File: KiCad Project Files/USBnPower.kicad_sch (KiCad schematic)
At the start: 11 parts, among them J1 SM04B, U3 XC6206PxxxMR, U4 PRTR5V0U2X

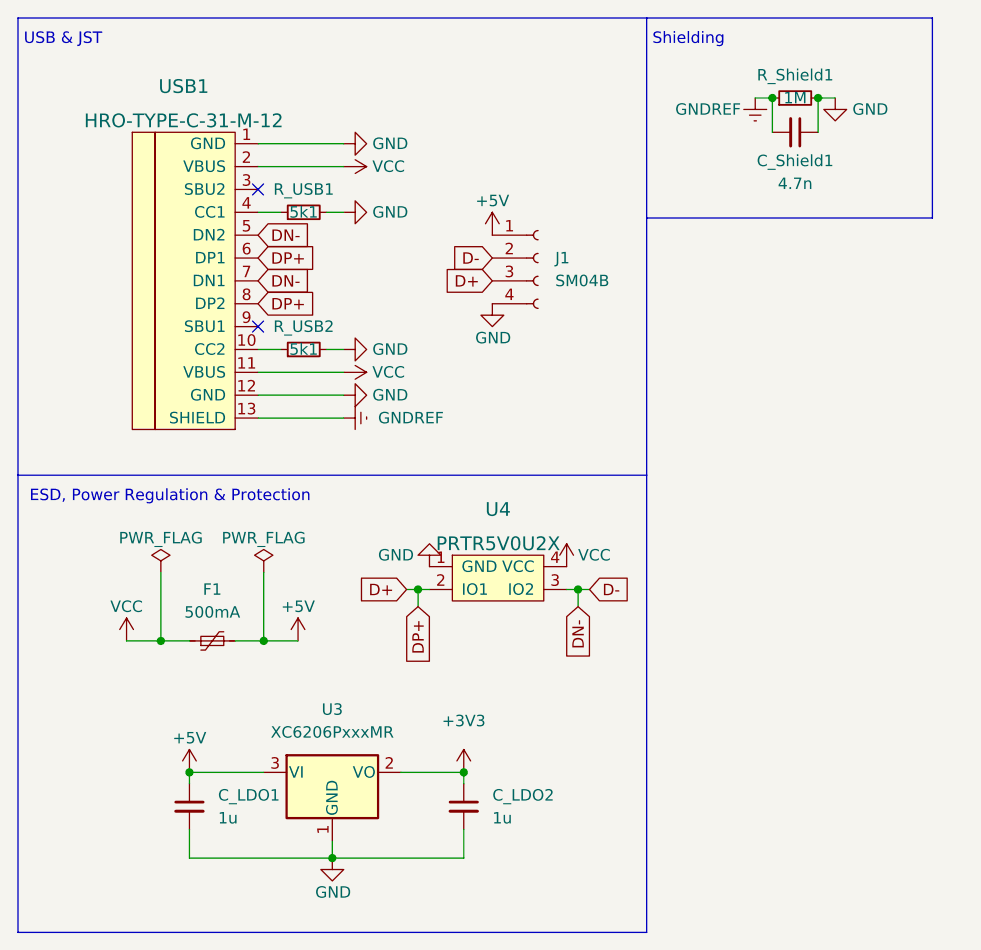
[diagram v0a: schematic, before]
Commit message: begin work on stm32 branch
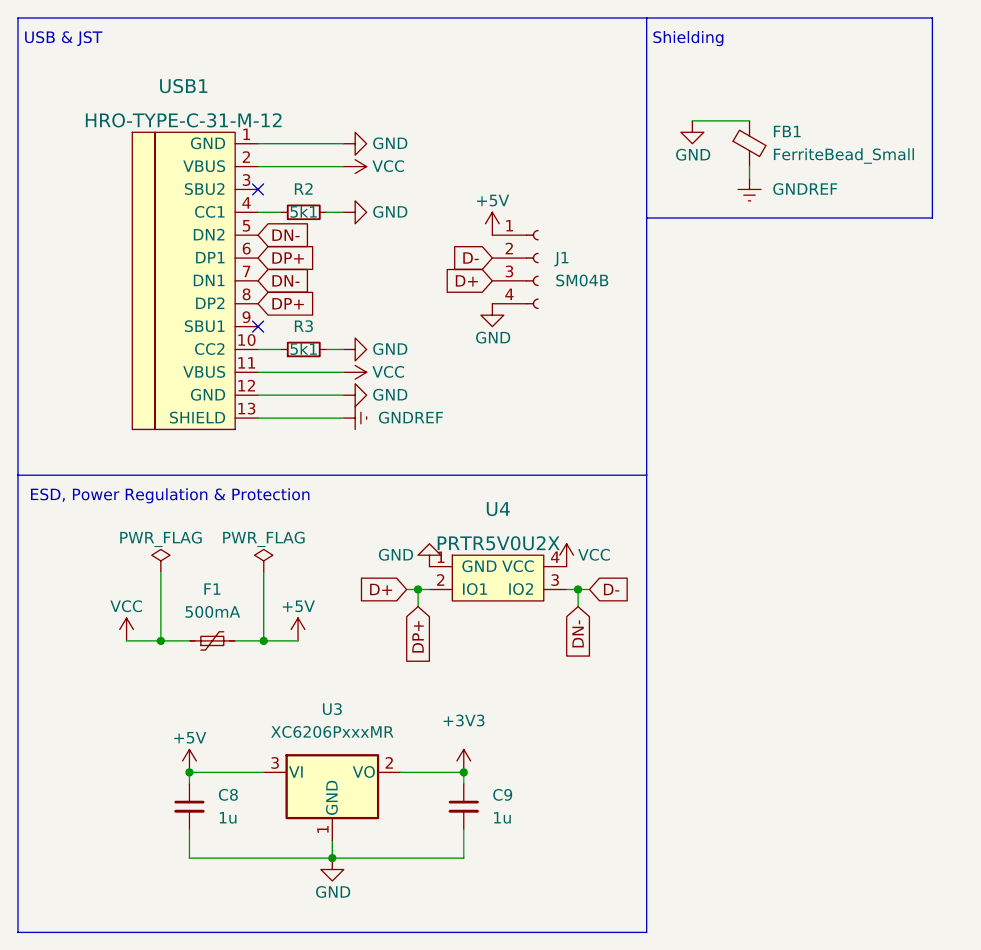
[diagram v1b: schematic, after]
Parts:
- removed C_Shield1: 4.7n, Capacitor_SMD:C_0402_1005Metric, symbol Device:C_Small
- removed R_Shield1: 1M, Resistor_SMD:R_0402_1005Metric, symbol Device:R_Small
- added FB1: FerriteBead_Small, Inductor_SMD:L_0805_2012Metric, symbol Device:FerriteBead_Small
- renumbered C_LDO1 to C8, C_LDO2 to C9, R_USB1 to R2, R_USB2 to R3
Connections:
- net GND: now also FB1.1
- net GNDREF: now also FB1.2
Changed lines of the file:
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@@
 (kicad_sch (version 20211123) (generator eeschema)
   (paper "A5")
-  (junction (at 96.52 21.59) (diameter 0) (color 0 0 0 0)
-  )
   (junction (at 40.005 81.915) (diameter 0) (color 0 0 0 0)
   )
@@
   )
   (junction (at 74.93 76.2) (diameter 0) (color 0 0 0 0)
-  )
-  (junction (at 101.6 21.59) (diameter 0) (color 0 0 0 0)
   )
   (junction (at 47.625 106.045) (diameter 0) (color 0 0 0 0)
@@
     (stroke (width 0) (type default) (color 0 0 0 0))
   )
-  (wire (pts (xy 96.52 21.59) (xy 96.52 25.4))
-    (stroke (width 0) (type default) (color 0 0 0 0))
-  )
   (wire (pts (xy 47.625 104.14) (xy 47.625 106.045))
     (stroke (width 0) (type default) (color 0 0 0 0))
@@
     (stroke (width 0) (type default) (color 0 0 0 0))
   )
-  (wire (pts (xy 101.6 21.59) (xy 101.6 25.4))
-    (stroke (width 0) (type default) (color 0 0 0 0))
-  )
   (polyline (pts (xy 12.7 12.7) (xy 12.7 63.5))
     (stroke (width 0) (type default) (color 0 0 0 0))
@@
     (stroke (width 0) (type default) (color 0 0 0 0))
   )
-  (wire (pts (xy 101.6 21.59) (xy 103.505 21.59))
-    (stroke (width 0) (type default) (color 0 0 0 0))
-  )
   (polyline (pts (xy 82.55 114.3) (xy 12.7 114.3))
     (stroke (width 0) (type default) (color 0 0 0 0))
@@
     (stroke (width 0) (type default) (color 0 0 0 0))
   )
-  (wire (pts (xy 94.615 21.59) (xy 96.52 21.59))
+  (wire (pts (xy 93.98 29.21) (xy 93.98 30.48))
     (stroke (width 0) (type default) (color 0 0 0 0))
   )
@@
   )
   (wire (pts (xy 74.93 76.2) (xy 76.2 76.2))
+    (stroke (width 0) (type default) (color 0 0 0 0))
+  )
+  (wire (pts (xy 87.63 24.13) (xy 93.98 24.13))
     (stroke (width 0) (type default) (color 0 0 0 0))
   )
@@
   (symbol (lib_id "Device:R_Small") (at 44.45 49.53 90) (unit 1)
     (in_bom yes) (on_board yes)
-    (property "Reference" "R_USB2" (id 0) (at 44.45 46.99 90))
+    (property "Reference" "R3" (id 0) (at 44.45 46.99 90))
     (property "Value" "5k1" (id 1) (at 44.45 49.53 90))
     (property "Footprint" "Resistor_SMD:R_0402_1005Metric" (id 2) (at 44.45 49.53 0)
@@
     (pin "2")
   )
-  (symbol (lib_id "power:GNDREF") (at 94.615 21.59 0) (unit 1)
-    (in_bom yes) (on_board yes)
-    (property "Reference" "#PWR0132" (id 0) (at 94.615 27.94 0)
-      (effects (font (size 1.27 1.27)) hide)
-    )
-    (property "Value" "GNDREF" (id 1) (at 85.725 22.86 0)
-      (effects (font (size 1.27 1.27)) (justify left))
-    )
-    (property "Footprint" "" (id 2) (at 94.615 21.59 0)
-      (effects (font (size 1.27 1.27)) hide)
-    )
-    (property "Datasheet" "" (id 3) (at 94.615 21.59 0)
-      (effects (font (size 1.27 1.27)) hide)
-    )
-    (pin "1")
-  )
   (symbol (lib_id "power:GND") (at 58.42 73.66 180) (unit 1)
     (in_bom yes) (on_board yes)
@@
   (symbol (lib_id "Device:R_Small") (at 44.45 34.29 90) (unit 1)
     (in_bom yes) (on_board yes)
-    (property "Reference" "R_USB1" (id 0) (at 44.45 31.75 90))
+    (property "Reference" "R2" (id 0) (at 44.45 31.75 90))
     (property "Value" "5k1" (id 1) (at 44.45 34.29 90))
     (property "Footprint" "Resistor_SMD:R_0402_1005Metric" (id 2) (at 44.45 34.29 0)
@@
     )
     (property "Datasheet" "" (id 3) (at 48.895 57.15 0)
+      (effects (font (size 1.27 1.27)) hide)
+    )
+    (pin "1")
+  )
+  (symbol (lib_id "Device:FerriteBead_Small") (at 93.98 26.67 0) (unit 1)
+    (in_bom yes) (on_board yes) (fields_autoplaced)
+    (property "Reference" "FB1" (id 0) (at 96.52 25.3618 0)
+      (effects (font (size 1.27 1.27)) (justify left))
+    )
+    (property "Value" "FerriteBead_Small" (id 1) (at 96.52 27.9018 0)
+      (effects (font (size 1.27 1.27)) (justify left))
+    )
+    (property "Footprint" "Inductor_SMD:L_0805_2012Metric" (id 2) (at 92.202 26.67 90)
+      (effects (font (size 1.27 1.27)) hide)
+    )
+    (property "Datasheet" "~" (id 3) (at 93.98 26.67 0)
+      (effects (font (size 1.27 1.27)) hide)
+    )
+    (pin "1")
+    (pin "2")
+  )
+  (symbol (lib_id "power:GNDREF") (at 93.98 30.48 0) (unit 1)
+    (in_bom yes) (on_board yes) (fields_autoplaced)
+    (property "Reference" "#PWR0109" (id 0) (at 93.98 36.83 0)
+      (effects (font (size 1.27 1.27)) hide)
+    )
+    (property "Value" "GNDREF" (id 1) (at 96.52 31.7499 0)
+      (effects (font (size 1.27 1.27)) (justify left))
+    )
+    (property "Footprint" "" (id 2) (at 93.98 30.48 0)
+      (effects (font (size 1.27 1.27)) hide)
+    )
+    (property "Datasheet" "" (id 3) (at 93.98 30.48 0)
       (effects (font (size 1.27 1.27)) hide)
     )
@@
     (pin "1")
   )
-  (symbol (lib_id "Device:C_Small") (at 99.06 25.4 270) (unit 1)
-    (in_bom yes) (on_board yes)
-    (property "Reference" "C_Shield1" (id 0) (at 99.06 28.575 90))
-    (property "Value" "4.7n" (id 1) (at 99.06 31.115 90))
-    (property "Footprint" "Capacitor_SMD:C_0402_1005Metric" (id 2) (at 99.06 25.4 0)
-      (effects (font (size 1.27 1.27)) hide)
-    )
-    (property "Datasheet" "~" (id 3) (at 99.06 25.4 0)
-      (effects (font (size 1.27 1.27)) hide)
-    )
-    (pin "1")
-    (pin "2")
+  (symbol (lib_id "power:GND") (at 87.63 24.13 0) (unit 1)
+    (in_bom yes) (on_board yes)
+    (property "Reference" "#PWR0110" (id 0) (at 87.63 30.48 0)
+      (effects (font (size 1.27 1.27)) hide)
+    )
+    (property "Value" "GND" (id 1) (at 85.725 27.94 0)
+      (effects (font (size 1.27 1.27)) (justify left))
+    )
+    (property "Footprint" "" (id 2) (at 87.63 24.13 0)
+      (effects (font (size 1.27 1.27)) hide)
+    )
+    (property "Datasheet" "" (id 3) (at 87.63 24.13 0)
+      (effects (font (size 1.27 1.27)) hide)
+    )
+    (pin "1")
   )
   (symbol (lib_id "power:GND") (at 48.895 34.29 90) (unit 1)
@@
   (symbol (lib_id "Device:C_Small") (at 31.75 100.33 0) (unit 1)
     (in_bom yes) (on_board yes) (fields_autoplaced)
-    (property "Reference" "C_LDO1" (id 0) (at 34.925 99.0662 0)
+    (property "Reference" "C8" (id 0) (at 34.925 99.0662 0)
       (effects (font (size 1.27 1.27)) (justify left))
     )
@@
     (pin "1")
     (pin "2")
-  )
-  (symbol (lib_id "power:GND") (at 103.505 21.59 0) (unit 1)
-    (in_bom yes) (on_board yes) (fields_autoplaced)
-    (property "Reference" "#PWR0131" (id 0) (at 103.505 27.94 0)
-      (effects (font (size 1.27 1.27)) hide)
-    )
-    (property "Value" "GND" (id 1) (at 105.41 22.8599 0)
-      (effects (font (size 1.27 1.27)) (justify left))
-    )
-    (property "Footprint" "" (id 2) (at 103.505 21.59 0)
-      (effects (font (size 1.27 1.27)) hide)
-    )
-    (property "Datasheet" "" (id 3) (at 103.505 21.59 0)
-      (effects (font (size 1.27 1.27)) hide)
-    )
-    (pin "1")
   )
   (symbol (lib_id "power:VCC") (at 24.765 81.915 0) (unit 1)
@@
     (pin "1")
   )
-  (symbol (lib_id "Device:R_Small") (at 99.06 21.59 90) (unit 1)
-    (in_bom yes) (on_board yes)
-    (property "Reference" "R_Shield1" (id 0) (at 99.06 19.05 90))
-    (property "Value" "1M" (id 1) (at 99.06 21.59 90))
-    (property "Footprint" "Resistor_SMD:R_0402_1005Metric" (id 2) (at 99.06 21.59 0)
-      (effects (font (size 1.27 1.27)) hide)
-    )
-    (property "Datasheet" "~" (id 3) (at 99.06 21.59 0)
-      (effects (font (size 1.27 1.27)) hide)
-    )
-    (pin "1")
-    (pin "2")
-  )
   (symbol (lib_id "Device:C_Small") (at 62.23 100.33 0) (unit 1)
     (in_bom yes) (on_board yes) (fields_autoplaced)
-    (property "Reference" "C_LDO2" (id 0) (at 65.405 99.0662 0)
-      (effects (font (size 1.27 1.27)) (justify left))
-    )
+    (property "Reference" "C9" (id 0) (at 65.405 99.0662 0)
+      (effects (font (size 1.27 1.27)) (justify left))
+    )
